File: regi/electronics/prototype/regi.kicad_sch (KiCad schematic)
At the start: 84 parts, among them J1 USB2UART, J2 1.47 IPS LCD, J3 ConnBattery, J4 RTD_PT100, Q1 SS8050, Q2 SS8050, Q3 SS8050, Q5 SS8050, SW1 RST, SW2 IN1, SW3 Boot, SW4 IN2, SW5 IN4, SW6 IN4, SW7 IN5, U1 CH340C, U2 ESP32-S3-WROOM-1, U3 TPS63001_SEPIC_3V3, U4 MAX31865xTP, U5 BQ24075RGT_DPPM, U7 BQ27421YZFR-G1A

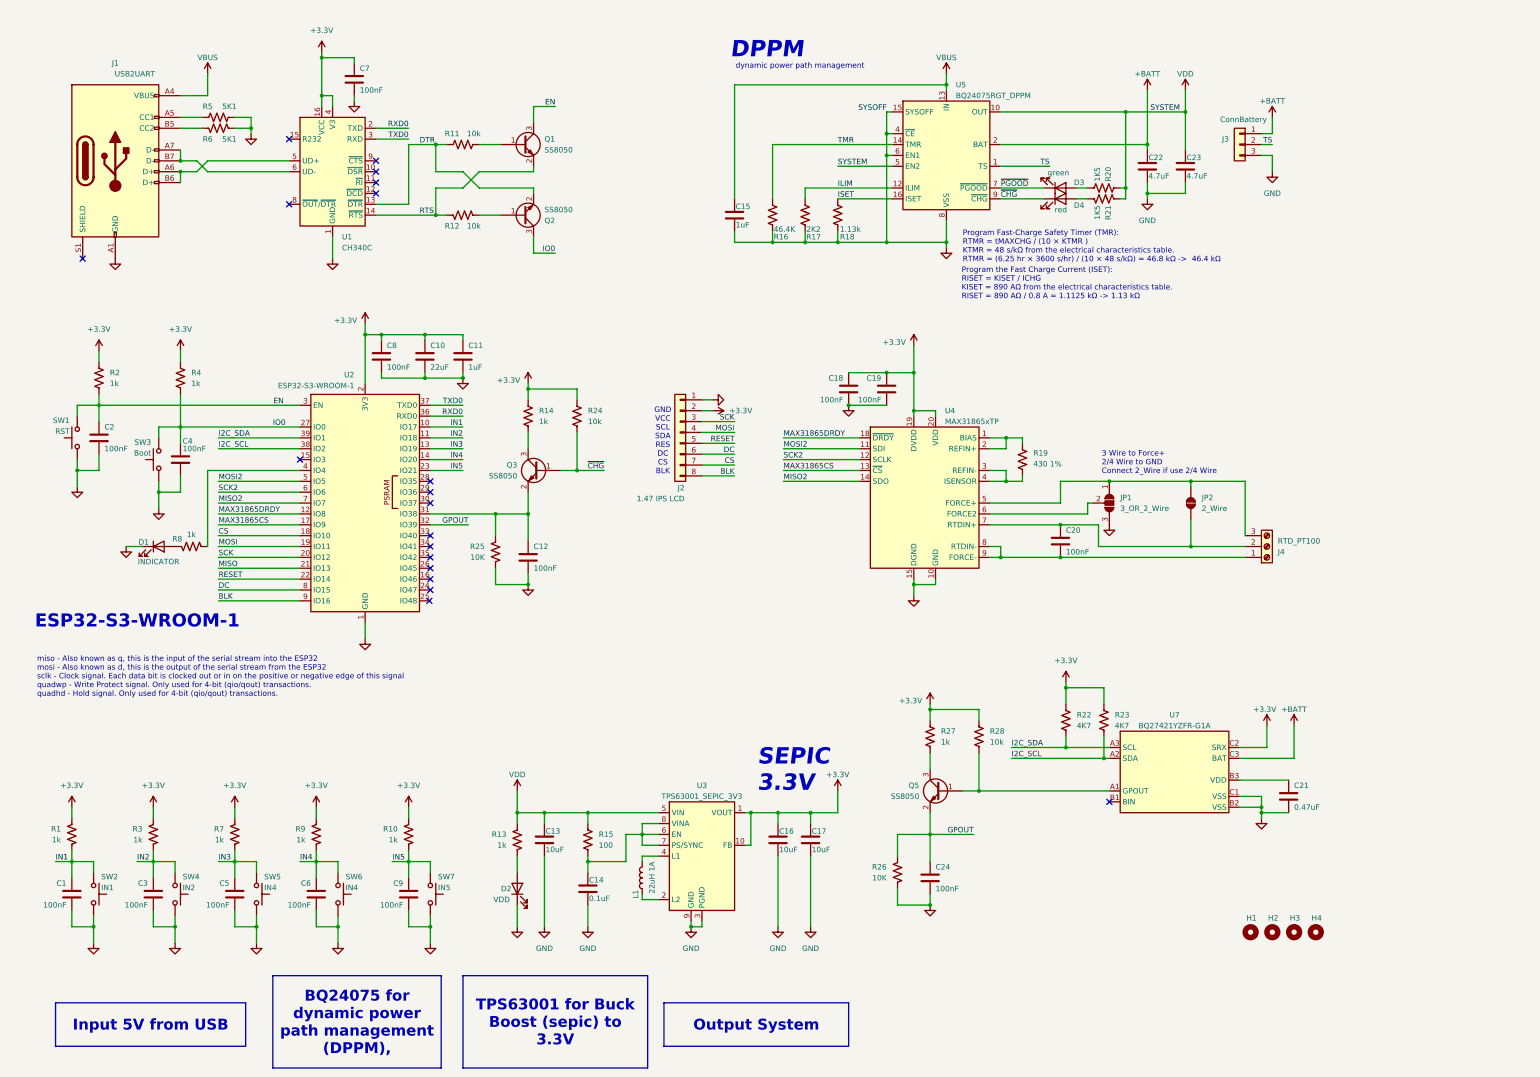
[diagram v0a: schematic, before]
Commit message: feat(regi): finished rough routing
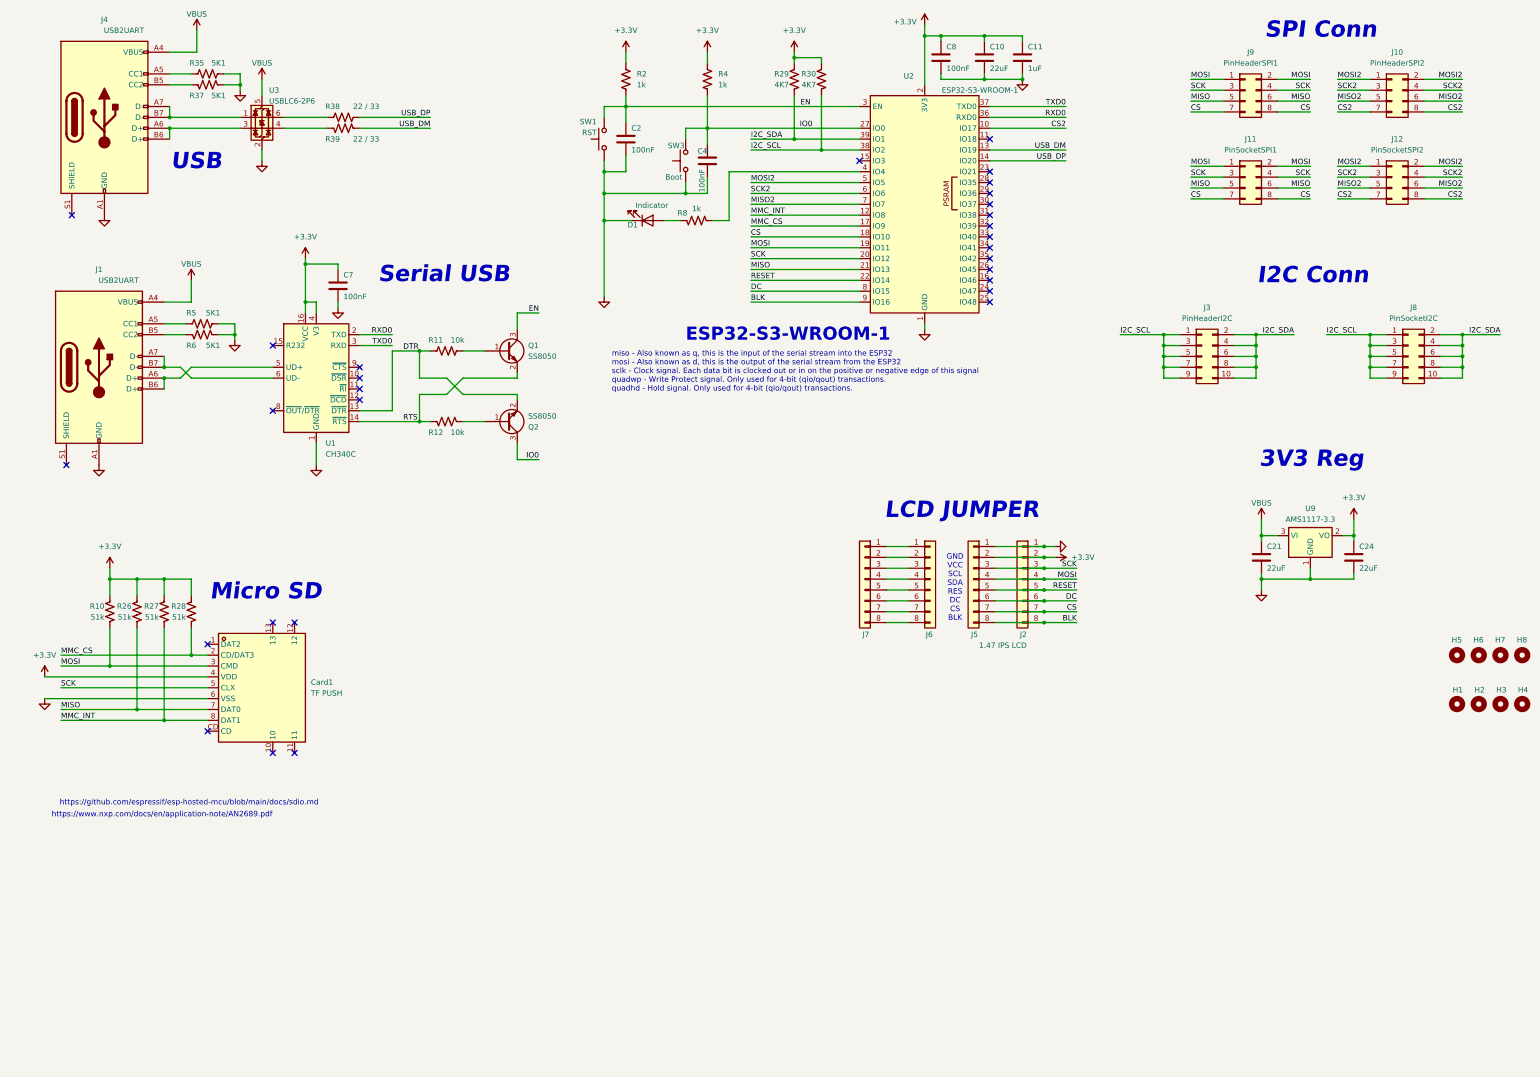
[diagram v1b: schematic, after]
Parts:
- removed C1, C12, C18, C19, C20, C3, C5, C6, C9: 100nF, Capacitor_SMD:C_0805_2012Metric_Pad1.18x1.45mm_HandSolder, symbol Device:C
- removed C13, C16, C17: 10uF, Capacitor_SMD:C_0805_2012Metric_Pad1.18x1.45mm_HandSolder, symbol Device:C
- removed C14: 0.1uF, Capacitor_SMD:C_0805_2012Metric_Pad1.18x1.45mm_HandSolder, symbol Device:C
- removed C15: 1uF, Capacitor_SMD:C_0805_2012Metric_Pad1.18x1.45mm_HandSolder, symbol Device:C
- removed C22, C23: 4.7uF, Capacitor_SMD:C_0805_2012Metric_Pad1.18x1.45mm_HandSolder, symbol Device:C
- removed D2: VDD, LED_SMD:LED_1206_3216Metric_Pad1.42x1.75mm_HandSolder, symbol Device:LED
- removed D3: green, LED_SMD:LED_0805_2012Metric_Pad1.15x1.40mm_HandSolder, symbol Device:LED
- removed D4: red, LED_SMD:LED_0805_2012Metric_Pad1.15x1.40mm_HandSolder, symbol Device:LED
- removed J3: ConnBattery, Connector_PinHeader_2.54mm:PinHeader_1x03_P2.54mm_Vertical, symbol Connector_Generic:Conn_01x03
- removed J4: RTD_PT100, TerminalBlock_Phoenix:TerminalBlock_Phoenix_PT-1,5-3-5.0-H_1x03_P5.00mm_Horizontal, symbol Connector:Screw_Terminal_01x03
- removed JP1: 3_OR_2_Wire, Jumper:SolderJumper-3_P1.3mm_Open_RoundedPad1.0x1.5mm, symbol Jumper:SolderJumper_3_Open
- removed JP2: 2_Wire, Jumper:SolderJumper-2_P1.3mm_Open_TrianglePad1.0x1.5mm, symbol Jumper:SolderJumper_2_Open
- removed L1: 22uH 1A, Inductor_SMD:L_Bourns_SRP7028A_7.3x6.6mm, symbol Device:L
- removed Q3, Q5: SS8050, Package_TO_SOT_SMD:SOT-23_Handsoldering, symbol Transistor_BJT:BC817
- removed R1, R13, R14, R3, R7, R9: 1k, Resistor_SMD:R_0805_2012Metric_Pad1.20x1.40mm_HandSolder, symbol Device:R_US
- removed R15: 100, Resistor_SMD:R_0805_2012Metric_Pad1.20x1.40mm_HandSolder, symbol Device:R_US
- removed R16: 46.4K, Resistor_SMD:R_0805_2012Metric_Pad1.20x1.40mm_HandSolder, symbol Device:R_US
- removed R17: 2K2, Resistor_SMD:R_0805_2012Metric_Pad1.20x1.40mm_HandSolder, symbol Device:R_US
- removed R18: 1.13k, Resistor_SMD:R_0805_2012Metric_Pad1.20x1.40mm_HandSolder, symbol Device:R_US
- removed R19: 430 1%, Resistor_SMD:R_0805_2012Metric_Pad1.20x1.40mm_HandSolder, symbol Device:R_US
- removed R20, R21: 1K5, Resistor_SMD:R_0805_2012Metric_Pad1.20x1.40mm_HandSolder, symbol Device:R_US
- removed R22, R23: 4K7, Resistor_SMD:R_0805_2012Metric_Pad1.20x1.40mm_HandSolder, symbol Device:R_US
- removed R24: 10k, Resistor_SMD:R_0805_2012Metric_Pad1.20x1.40mm_HandSolder, symbol Device:R_US
- removed R25: 10K, Resistor_SMD:R_0805_2012Metric_Pad1.20x1.40mm_HandSolder, symbol Device:R_US
- removed SW2: IN1, Button_Switch_SMD:SW_SPST_Omron_B3FS-100xP, symbol Switch:SW_Push
- removed SW4: IN2, Button_Switch_SMD:SW_SPST_Omron_B3FS-100xP, symbol Switch:SW_Push
- removed SW5, SW6: IN4, Button_Switch_SMD:SW_SPST_Omron_B3FS-100xP, symbol Switch:SW_Push
- removed SW7: IN5, Button_Switch_SMD:SW_SPST_Omron_B3FS-100xP, symbol Switch:SW_Push
- removed U3: TPS63001_SEPIC_3V3, Package_SON:Texas_DRC0010J_ThermalVias, symbol Regulator_Switching:TPS63001
- removed U4: MAX31865xTP, Package_DFN_QFN:TQFN-20-1EP_5x5mm_P0.65mm_EP3.25x3.25mm, symbol Sensor_Temperature:MAX31865xTP
- removed U5: BQ24075RGT_DPPM, Package_DFN_QFN:VQFN-16-1EP_3x3mm_P0.5mm_EP1.6x1.6mm, symbol Battery_Management:BQ24075RGT
- removed U7: BQ27421YZFR-G1A, easyeda2kicad:DSBGA-9_L1.5-W1.5-R3-C3-P0.50-BL, symbol easyeda2kicad:BQ27421YZFR-G1A
- added Card1: TF PUSH, easyeda2kicad:TF-SMD_TF-PUSH, symbol easyeda2kicad:TFPUSH
- added H5, H6, H7, H8: MountingHole, MountingHole:MountingHole_3.2mm_M3, symbol Mechanical:MountingHole
- added J10: PinHeaderSPI2, Connector_PinHeader_2.54mm:PinHeader_2x04_P2.54mm_Vertical, symbol Connector_Generic:Conn_02x04_Odd_Even
- added J11: PinSocketSPI1, Connector_PinHeader_2.54mm:PinHeader_2x04_P2.54mm_Vertical, symbol Connector_Generic:Conn_02x04_Odd_Even
- added J12: PinSocketSPI2, Connector_PinHeader_2.54mm:PinHeader_2x04_P2.54mm_Vertical, symbol Connector_Generic:Conn_02x04_Odd_Even
- added J3: PinHeaderI2C, Connector_PinHeader_2.54mm:PinHeader_2x05_P2.54mm_Vertical, symbol Connector_Generic:Conn_02x05_Odd_Even
- added J4: USB2UART, Connector_USB:USB_C_Receptacle_GCT_USB4110, symbol Connector:USB_C_Receptacle_USB2.0_14P
- added J5, J6, J7: lcd jumper, Connector_PinHeader_2.54mm:PinHeader_1x08_P2.54mm_Vertical, symbol Connector_Generic:Conn_01x08
- added J8: PinSocketI2C, Connector_PinSocket_2.54mm:PinSocket_2x05_P2.54mm_Vertical, symbol Connector_Generic:Conn_02x05_Odd_Even
- added J9: PinHeaderSPI1, Connector_PinHeader_2.54mm:PinHeader_2x04_P2.54mm_Vertical, symbol Connector_Generic:Conn_02x04_Odd_Even
- added R29, R30: 4K7, Resistor_SMD:R_0805_2012Metric_Pad1.20x1.40mm_HandSolder, symbol Device:R_US
- added R35, R37: 5K1, Resistor_SMD:R_0805_2012Metric_Pad1.20x1.40mm_HandSolder, symbol Device:R_US
- added R38, R39: 22 / 33, Resistor_SMD:R_0805_2012Metric_Pad1.20x1.40mm_HandSolder, symbol Device:R_US
- added U3: USBLC6-2P6, Package_TO_SOT_SMD:SOT-666, symbol Power_Protection:USBLC6-2P6
- added U9: AMS1117-3.3, Package_TO_SOT_SMD:SOT-223-3_TabPin2, symbol Regulator_Linear:AMS1117-3.3
- C21: value 0.47uF -> 22uF
- C24: value 100nF -> 22uF
- D1: value INDICATOR -> Indicator
- R10, R27: value 1k -> 51k
- R26: value 10K -> 51k
- R28: value 10k -> 51k
- SW1, SW3: footprint Button_Switch_SMD:SW_SPST_PTS810 -> Button_Switch_SMD:SW_SPST_EVQP7A
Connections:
- net MAX31865CS is gone; now on net MMC_CS: U2.17 (IO9)
- net MAX31865DRDY is gone; now on net MMC_INT: U2.12 (IO8)
- net +3.3V: now also C24.1, R26.1, Card1.4 (VDD), J5.2 (Pin_2), R29.1, R30.1, U9.2 (VO)
- net BLK: now also J5.8 (Pin_8)
- net CS: now also J11.7 (Pin_7), J11.8 (Pin_8), J5.7 (Pin_7), J9.7 (Pin_7), J9.8 (Pin_8)
- net DC: now also J5.6 (Pin_6)
- net GND: now also Card1.6 (VSS), J4.A1 (GND), J4.A12 (GND), J4.B1 (GND), J4.B12 (GND), J5.1 (Pin_1), R35.1, R37.1, U3.2 (GND), U9.1 (GND); no longer R26.2
- net I2C_SCL: now also J3.1 (Pin_1), J3.3 (Pin_3), J3.5 (Pin_5), J3.7 (Pin_7), J3.9 (Pin_9), J8.1 (Pin_1), J8.3 (Pin_3), J8.5 (Pin_5), J8.7 (Pin_7), J8.9 (Pin_9), R30.2
- net I2C_SDA: now also J3.10 (Pin_10), J3.2 (Pin_2), J3.4 (Pin_4), J3.6 (Pin_6), J3.8 (Pin_8), J8.10 (Pin_10), J8.2 (Pin_2), J8.4 (Pin_4), J8.6 (Pin_6), J8.8 (Pin_8), R29.2
- net MISO: now also R26.2, Card1.7 (DAT0), J11.5 (Pin_5), J11.6 (Pin_6), J9.5 (Pin_5), J9.6 (Pin_6)
- net MISO2: now also J10.5 (Pin_5), J10.6 (Pin_6), J12.5 (Pin_5), J12.6 (Pin_6)
- net MOSI: now also R10.2, Card1.3 (CMD), J11.1 (Pin_1), J11.2 (Pin_2), J5.4 (Pin_4), J9.1 (Pin_1), J9.2 (Pin_2)
- net MOSI2: now also J10.1 (Pin_1), J10.2 (Pin_2), J12.1 (Pin_1), J12.2 (Pin_2)
- net RESET: now also J5.5 (Pin_5)
- net SCK: now also Card1.5 (CLX), J11.3 (Pin_3), J11.4 (Pin_4), J5.3 (Pin_3), J9.3 (Pin_3), J9.4 (Pin_4)
- net SCK2: now also J10.3 (Pin_3), J10.4 (Pin_4), J12.3 (Pin_3), J12.4 (Pin_4)
- net VBUS: now also C21.1, J4.A4 (VBUS), J4.A9 (VBUS), J4.B4 (VBUS), J4.B9 (VBUS), U3.5 (VBUS), U9.3 (VI)
- net MMC_CS: now reaches R28.2
- net MMC_CS: now also Card1.2 (CD/DAT3)
- net MMC_INT: now reaches R27.2
- net MMC_INT: now also Card1.8 (DAT1)
- removed net GPOUT: C24.1, R26.1, U2.32 (IO39)
- net IN1 renamed CS2
- net CS2: now also J10.7 (Pin_7), J10.8 (Pin_8), J12.7 (Pin_7), J12.8 (Pin_8)
- net IN2: no longer names the net of U2.11 (IO18)
- net IN3 renamed USB_DM
- net USB_DM: now also R39.1
- net IN4 renamed USB_DP
- net USB_DP: now also R38.1
- net IN5: no longer names the net of U2.23 (IO21)
- net IN5: no longer R10.2
- new net: J4.A7 (D-), J4.B7 (D-), U3.1 (I/O1)
- new net: J4.A6 (D+), J4.B6 (D+), U3.3 (I/O2)
- new net: R39.2, U3.4 (I/O2)
- new net: R38.2, U3.6 (I/O1)
- new net: J6.1 (Pin_1), J7.1 (Pin_1)
- new net: J6.2 (Pin_2), J7.2 (Pin_2)
- new net: J6.3 (Pin_3), J7.3 (Pin_3)
- new net: J6.4 (Pin_4), J7.4 (Pin_4)
- new net: J6.5 (Pin_5), J7.5 (Pin_5)
- new net: J6.6 (Pin_6), J7.6 (Pin_6)
- new net: J6.7 (Pin_7), J7.7 (Pin_7)
- new net: J6.8 (Pin_8), J7.8 (Pin_8)
- new net: J4.A5 (CC1), R35.2
- new net: J4.B5 (CC2), R37.2
- no-connect marks 19 -> 29
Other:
- note added: "3V3 Reg"
- note added: "I2C Conn"
- note added: "LCD JUMPER"
- note added: "Micro SD"
- note added: "SPI Conn"
- note added: "Serial USB"
- note added: "USB"
- note added: "https://github.com/espressif/esp-hosted-mcu/blob/main/docs/sdio.md"
- note added: "https://www.nxp.com/docs/en/application-note/AN2689.pdf"
- note removed: "3 Wire to Force+ 2/4 Wire to GND Connect 2_Wire if use 2/4 Wire"
- note removed: "DPPM"
- note removed: "Program Fast-Charge Safety Timer (TMR): RTMR = tMAXCHG / (10 × KTMR ) KTMR = 48 s/kΩ from the electrical characteristics table. RTMR = (6.25 hr × 3600 s/hr) / (10 × 48 s/kΩ) = 46.8 kΩ -> 46.4 kΩ"
- note removed: "Program the Fast Charge Current (ISET): RISET = KISET / ICHG KISET = 890 AΩ from the electrical characteristics table. RISET = 890 AΩ / 0.8 A = 1.1125 kΩ -> 1.13 kΩ"
- note removed: "SEPIC 3.3V"
- note removed: "dynamic power path management"
- title: Temperature Measurement Dongle -> REGI REPL - Proto 1
